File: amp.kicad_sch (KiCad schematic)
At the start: 32 parts, among them J10 JST_SH_1x4_SM04B-SRSS-TB-LF-SN, J4 PinHeader_1x2_P2.54mm_Drill1.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, J5 Phone_TRS_MiniJack_SJ-3523-SM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, J9 JST_SUR_1x5_BM05B-SURS-TB-LF-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, U3 TAS2505IRGER, Y2 Oscillator_50MHz_ECS_1612MV

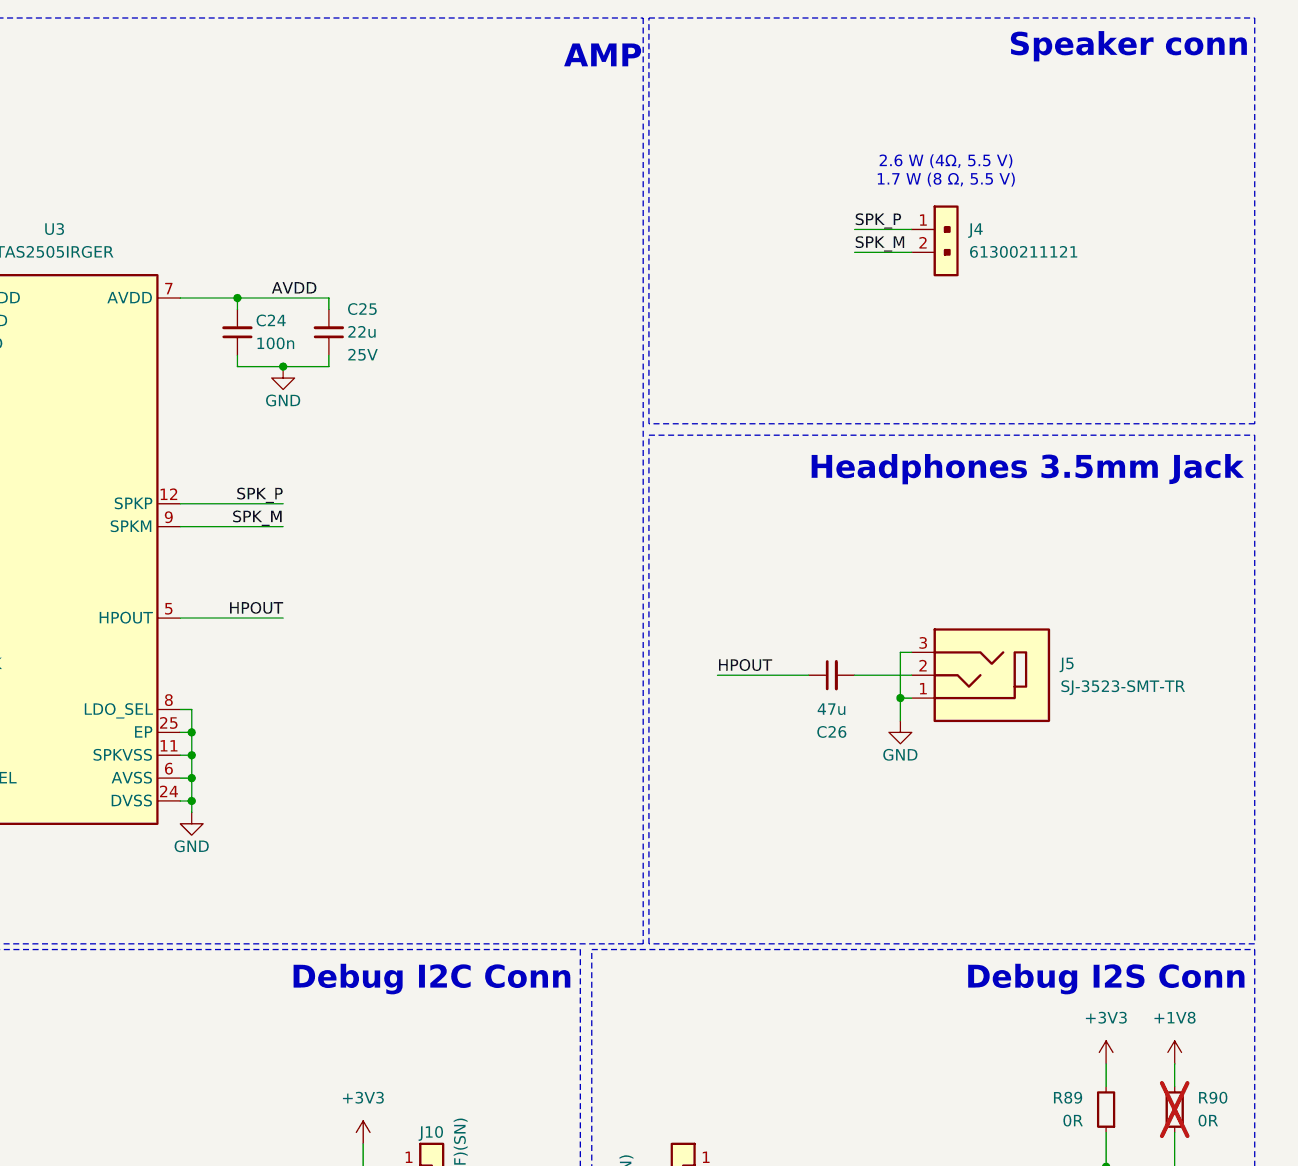
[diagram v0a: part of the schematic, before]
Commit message: [#71555] Expand sch logic areas naming
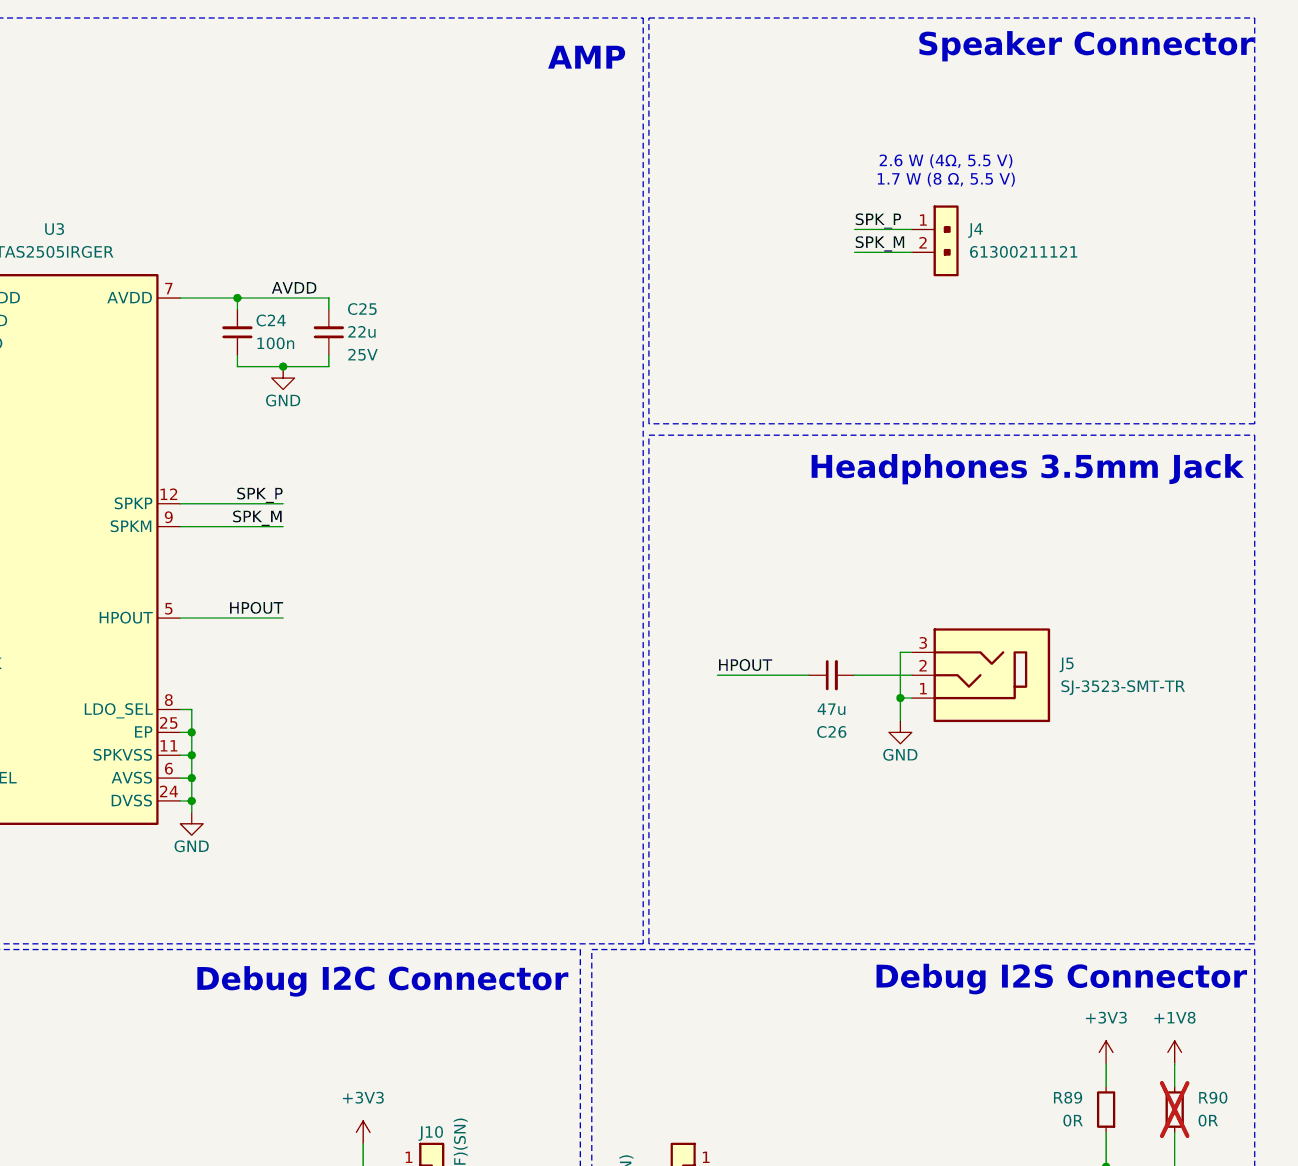
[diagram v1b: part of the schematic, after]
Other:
- note added: "Debug I2C Connector"
- note added: "Debug I2S Connector"
- note added: "Speaker Connector"
- note removed: "Debug I2C Conn"
- note removed: "Debug I2S Conn"
- note removed: "Speaker conn"
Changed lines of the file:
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@@
 		)
 	)
-	(text "Speaker conn"
+	(text "Speaker Connector"
 		(exclude_from_sim no)
-		(at 318.77 74.93 0)
+		(at 313.944 74.93 0)
 		(effects
 			(font
@@
 	(text "AMP"
 		(exclude_from_sim no)
-		(at 260.35 76.2 0)
+		(at 258.572 76.454 0)
 		(effects
 			(font
@@
 		)
 	)
-	(text "Debug I2C Conn"
+	(text "Debug I2C Connector"
 		(exclude_from_sim no)
-		(at 241.3 178.562 0)
+		(at 235.712 178.816 0)
 		(effects
 			(font
@@
 		)
 	)
-	(text "Debug I2S Conn"
+	(text "Debug I2S Connector"
 		(exclude_from_sim no)
-		(at 316.23 178.562 0)
+		(at 311.15 178.562 0)
 		(effects
 			(font

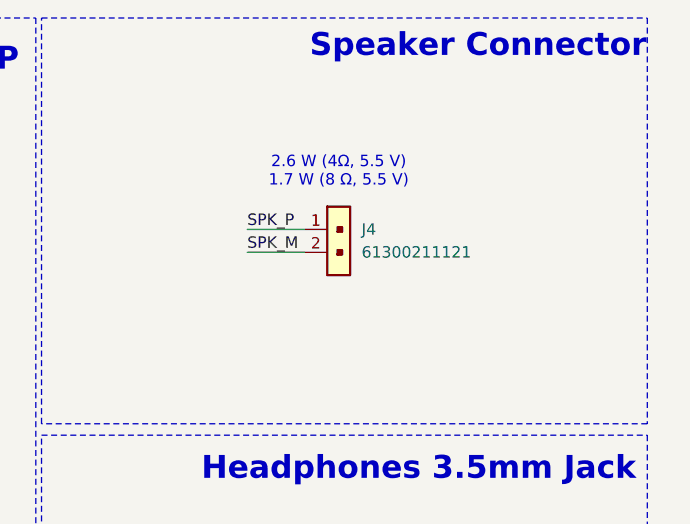
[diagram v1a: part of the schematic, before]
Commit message: [#71555] Add NPTH and change speaker connector to JST XH
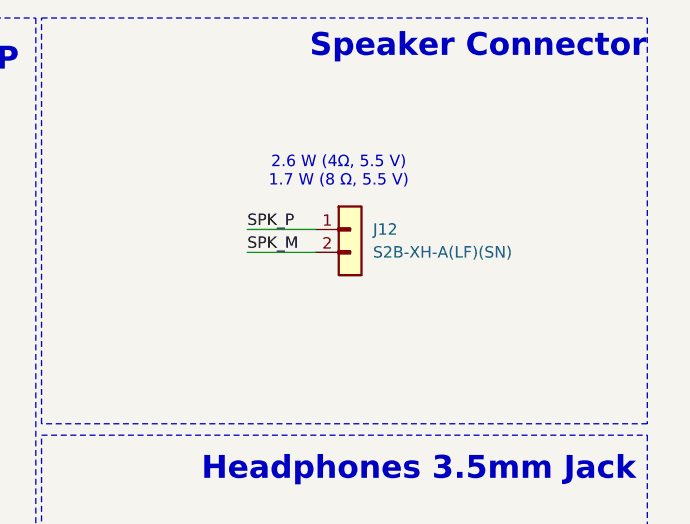
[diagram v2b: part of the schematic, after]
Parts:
- removed J4: PinHeader_1x2_P2.54mm_Drill1.1mm, antmicro-footprints:PinHeader_1x2_P2.54_Drill1.1mm, symbol antmicroGenericPinHeaders:PinHeader_1x2_P2.54mm_Drill1.1mm
- added J12: JST_XH_1x2_S2B-XH-A-LF-SN, antmicro-footprints:Conn_JST_XH_1x2_S2B-XH-A-LF-SN, symbol antmicroWire2BoardConnectors:JST_XH_1x2_S2B-XH-A-LF-SN
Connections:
- net SPK_M: now also J12.2
- net SPK_P: now also J12.1
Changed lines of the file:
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@@
 	(wire
 		(pts
-			(xy 288.29 97.79) (xy 294.64 97.79)
+			(xy 288.29 97.79) (xy 295.91 97.79)
 		)
 		(stroke
@@
 	(wire
 		(pts
-			(xy 288.29 95.25) (xy 294.64 95.25)
+			(xy 288.29 95.25) (xy 295.91 95.25)
 		)
 		(stroke
@@
 	)
 	(symbol
+		(lib_id "antmicroWire2BoardConnectors:JST_XH_1x2_S2B-XH-A-LF-SN")
+		(at 295.91 95.25 0)
+		(unit 1)
+		(exclude_from_sim no)
+		(in_bom yes)
+		(on_board yes)
+		(dnp no)
+		(fields_autoplaced yes)
+		(property "Reference" "J12"
+			(at 302.26 95.25 0)
+			(effects
+				(font
+					(size 1.27 1.27)
+					(thickness 0.15)
+				)
+				(justify left)
+			)
+		)
+		(property "Value" "JST_XH_1x2_S2B-XH-A-LF-SN"
+			(at 321.31 105.41 0)
+			(effects
+				(font
+					(size 1.27 1.27)
+					(thickness 0.15)
+				)
+				(justify left bottom)
+				(hide yes)
+			)
+		)
+		(property "Footprint" "antmicro-footprints:Conn_JST_XH_1x2_S2B-XH-A-LF-SN"
+			(at 321.31 107.95 0)
+			(effects
+				(font
+					(size 1.27 1.27)
+					(thickness 0.15)
+				)
+				(justify left bottom)
+				(hide yes)
+			)
+		)
+		(property "Datasheet" "https://www.tme.eu/Document/0a99312bb6c67d3f0f7869fe9a023cea/XH.pdf"
+			(at 321.31 110.49 0)
+			(effects
+				(font
+					(size 1.27 1.27)
+					(thickness 0.15)
+				)
+				(justify left bottom)
+				(hide yes)
+			)
+		)
+		(property "Description" "Connector Header Through Hole, Right Angle 2 position 0.098\" (2.50mm)"
+			(at 295.91 95.25 0)
+			(effects
+				(font
+					(size 1.27 1.27)
+				)
+				(hide yes)
+			)
+		)
+		(property "MPN" "S2B-XH-A(LF)(SN)"
+			(at 302.26 97.79 0)
+			(effects
+				(font
+					(size 1.27 1.27)
+					(thickness 0.15)
+				)
+				(justify left)
+			)
+		)
+		(property "Manufacturer" "JST Automotive Connectors"
+			(at 321.31 102.87 0)
+			(effects
+				(font
+					(size 1.27 1.27)
+					(thickness 0.15)
+				)
+				(justify left bottom)
+				(hide yes)
+			)
+		)
+		(property "Author" "Antmicro"
+			(at 321.31 113.03 0)
+			(effects
+				(font
+					(size 1.27 1.27)
+					(thickness 0.15)
+				)
+				(justify left bottom)
+				(hide yes)
+			)
+		)
+		(property "License" "Apache-2.0"
+			(at 321.31 115.57 0)
+			(effects
+				(font
+					(size 1.27 1.27)
+					(thickness 0.15)
+				)
+				(justify left bottom)
+				(hide yes)
+			)
+		)
+		(pin "2"
+		)
+		(pin "1"
+		)
+		(instances
+			(project ""
+				(path "/7fb12ebf-f685-4412-b638-445b1bf344bc/80300fa7-dce3-4149-8e27-6609cbfb608d"
+					(reference "J12")
+					(unit 1)
+				)
+			)
+		)
+	)
+	(symbol
 		(lib_id "antmicroResistors0402:R_0R_0402")
 		(at 175.26 125.73 180)
@@
 					(unit 1)
 				)
-			)
-		)
-	)
-	(symbol
-		(lib_id "antmicroGenericPinHeaders:PinHeader_1x2_P2.54mm_Drill1.1mm")
-		(at 294.64 95.25 0)
-		(unit 1)
-		(exclude_from_sim no)
-		(in_bom yes)
-		(on_board yes)
-		(dnp no)
-		(fields_autoplaced yes)
-		(property "Reference" "J4"
-			(at 300.99 95.25 0)
-			(effects
-				(font
-					(size 1.27 1.27)
-					(thickness 0.15)
-				)
-				(justify left)
-			)
-		)
-		(property "Value" "PinHeader_1x2_P2.54mm_Drill1.1mm"
-			(at 314.96 102.87 0)
-			(effects
-				(font
-					(size 1.27 1.27)
-					(thickness 0.15)
-				)
-				(justify left bottom)
-				(hide yes)
-			)
-		)
-		(property "Footprint" "antmicro-footprints:PinHeader_1x2_P2.54_Drill1.1mm"
-			(at 314.96 105.41 0)
-			(effects
-				(font
-					(size 1.27 1.27)
-					(thickness 0.15)
-				)
-				(justify left bottom)
-				(hide yes)
-			)
-		)
-		(property "Datasheet" "https://katalog.we-online.de/em/datasheet/6130xx11121.pdf"
-			(at 314.96 107.95 0)
-			(effects
-				(font
-					(size 1.27 1.27)
-					(thickness 0.15)
-				)
-				(justify left bottom)
-				(hide yes)
-			)
-		)
-		(property "Description" "Pin Header, Vertical, Board-to-Board, 2.54 mm, 1 Rows, 2 Contacts, Through Hole Straight, WR-PHD"
-			(at 294.64 95.25 0)
-			(effects
-				(font
-					(size 1.27 1.27)
-				)
-				(hide yes)
-			)
-		)
-		(property "MPN" "61300211121"
-			(at 300.99 97.79 0)
-			(effects
-				(font
-					(size 1.27 1.27)
-					(thickness 0.15)
-				)
-				(justify left)
-			)
-		)
-		(property "Manufacturer" "Würth Elektronik"
-			(at 314.96 113.03 0)
-			(effects
-				(font
-					(size 1.27 1.27)
-					(thickness 0.15)
-				)
-				(justify left bottom)
-				(hide yes)
-			)
-		)
-		(property "Author" "Antmicro"
-			(at 314.96 115.57 0)
-			(effects
-				(font
-					(size 1.27 1.27)
-					(thickness 0.15)
-				)
-				(justify left bottom)
-				(hide yes)
-			)
-		)
-		(property "License" "Apache-2.0"
-			(at 314.96 118.11 0)
-			(effects
-				(font
-					(size 1.27 1.27)
-					(thickness 0.15)
-				)
-				(justify left bottom)
-				(hide yes)
-			)
-		)
-		(pin "1"
-		)
-		(pin "2"
-		)
-		(instances
-			(project ""
-				(path "/7fb12ebf-f685-4412-b638-445b1bf344bc/80300fa7-dce3-4149-8e27-6609cbfb608d"
-					(reference "J4")
-					(unit 1)
-				)
